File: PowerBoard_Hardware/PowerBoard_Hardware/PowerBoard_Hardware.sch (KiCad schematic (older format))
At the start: 12 parts

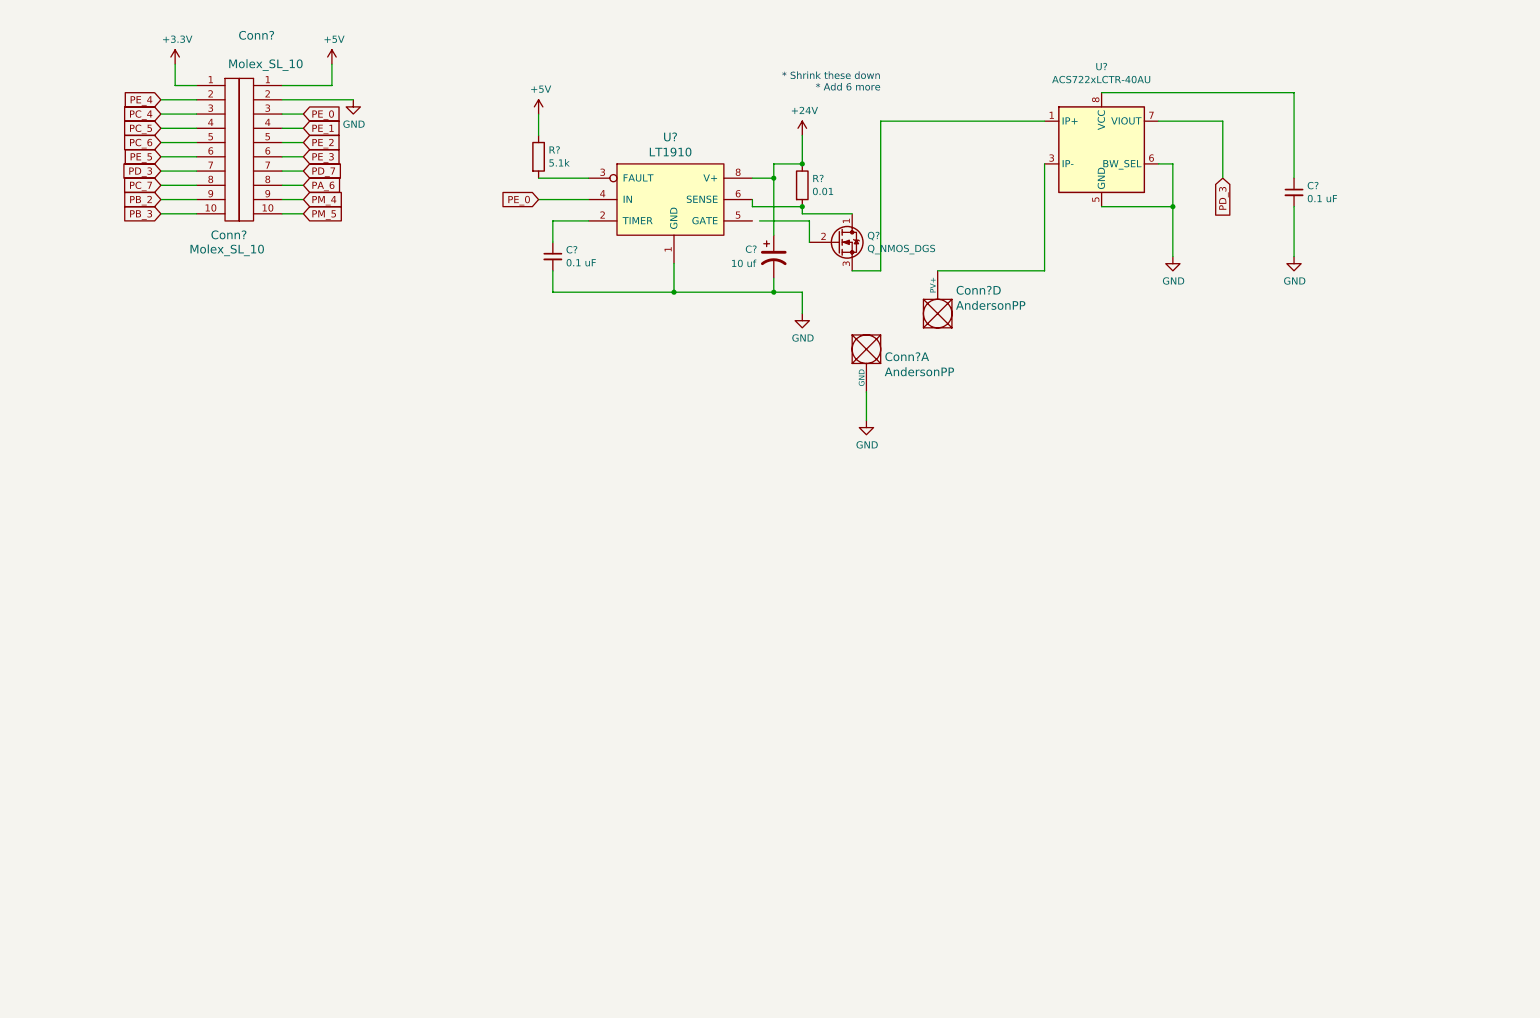
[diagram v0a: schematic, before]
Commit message: Pass 1.2
*Circuit has been consolidated
*All 6 circuits have been added
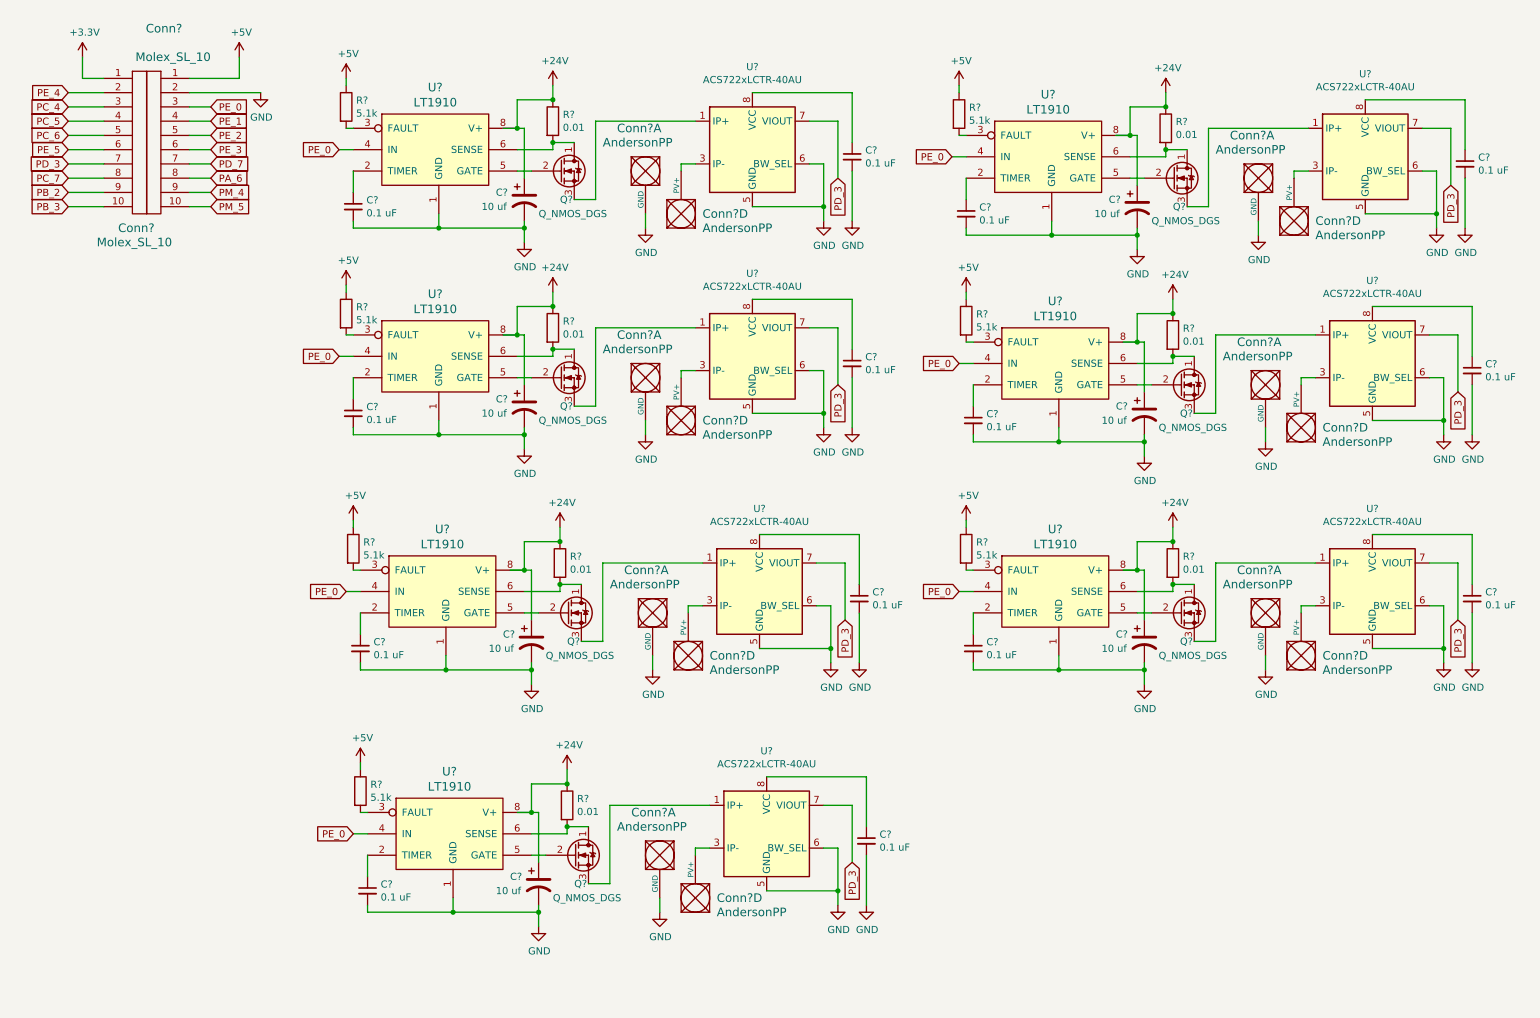
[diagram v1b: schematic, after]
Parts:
- added C? (x12): 0.1 uF, symbol Device:C_Small
- added C? (x6): 10 uf, symbol Device:CP1
- added Conn? (x12): AndersonPP, symbol MRDT_Connectors:AndersonPP
- added Q? (x6): Q_NMOS_DGS, symbol Device:Q_NMOS_DGS
- added R? (x6): 5.1k, symbol Device:R
- added R? (x6): 0.01, symbol Device:R
- added U? (x6): ACS722xLCTR-40AU, Package_SO:SOIC-8_3.9x4.9mm_P1.27mm, symbol Sensor_Current:ACS722xLCTR-40AU
- added U? (x6): LT1910, symbol MRDT_ICs:LT1910
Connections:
- net +24V: now also C?.1, C?.1, C?.1, C?.1, C?.1, C?.1, R?.1, R?.1, R?.1, R?.1, R?.1, R?.1, U?.8 (V+), U?.8 (V+), U?.8 (V+), U?.8 (V+), U?.8 (V+), U?.8 (V+)
- net +5V: now also R?.1, R?.1, R?.1, R?.1, R?.1, R?.1
- net GND: now also C?.2, C?.2, C?.2, C?.2, C?.2, C?.2, C?.2, C?.2, C?.2, C?.2, C?.2, C?.2, C?.2, C?.2, C?.2, C?.2, C?.2, C?.2, Conn?.1 (GND), Conn?.1 (GND), Conn?.1 (GND), Conn?.1 (GND), Conn?.1 (GND), Conn?.1 (GND), U?.1 (GND), U?.1 (GND), U?.1 (GND), U?.1 (GND), U?.1 (GND), U?.1 (GND), U?.5 (GND), U?.5 (GND), U?.5 (GND), U?.5 (GND), U?.5 (GND), U?.5 (GND), U?.6 (BW_SEL), U?.6 (BW_SEL), U?.6 (BW_SEL), U?.6 (BW_SEL), U?.6 (BW_SEL), U?.6 (BW_SEL)
- net PD_3: now also U?.7 (VIOUT), U?.7 (VIOUT), U?.7 (VIOUT), U?.7 (VIOUT), U?.7 (VIOUT), U?.7 (VIOUT)
- net PE_0: now also U?.4 (IN), U?.4 (IN), U?.4 (IN), U?.4 (IN), U?.4 (IN), U?.4 (IN)
- net at U?.5 (GATE): now also Q?.2 (G)
- new net: Q?.3 (S), U?.1 (IP+), U?.2 (IP+) (x6)
- new net: Conn?.4 (PV+), U?.3 (IP-), U?.4 (IP-) (x6)
- new net: C?.1, U?.8 (VCC) (x6)
- new net: R?.2, U?.3 (FAULT) (x6)
- new net: Q?.1 (D), R?.2, U?.6 (SENSE) (x6)
- new net: C?.1, U?.2 (TIMER) (x6)
- new net: Q?.2 (G), U?.5 (GATE) (x6)
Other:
- note removed: "* Shrink these down\n* Add 6 more\n"
- moved on the sheet: C?, Conn?, Conn?A, Conn?D, Q?, R?, U?

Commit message: Pass 1.3
*+24v replaced with VDD
*Analog pins assigned
*global PV Andersons assigned
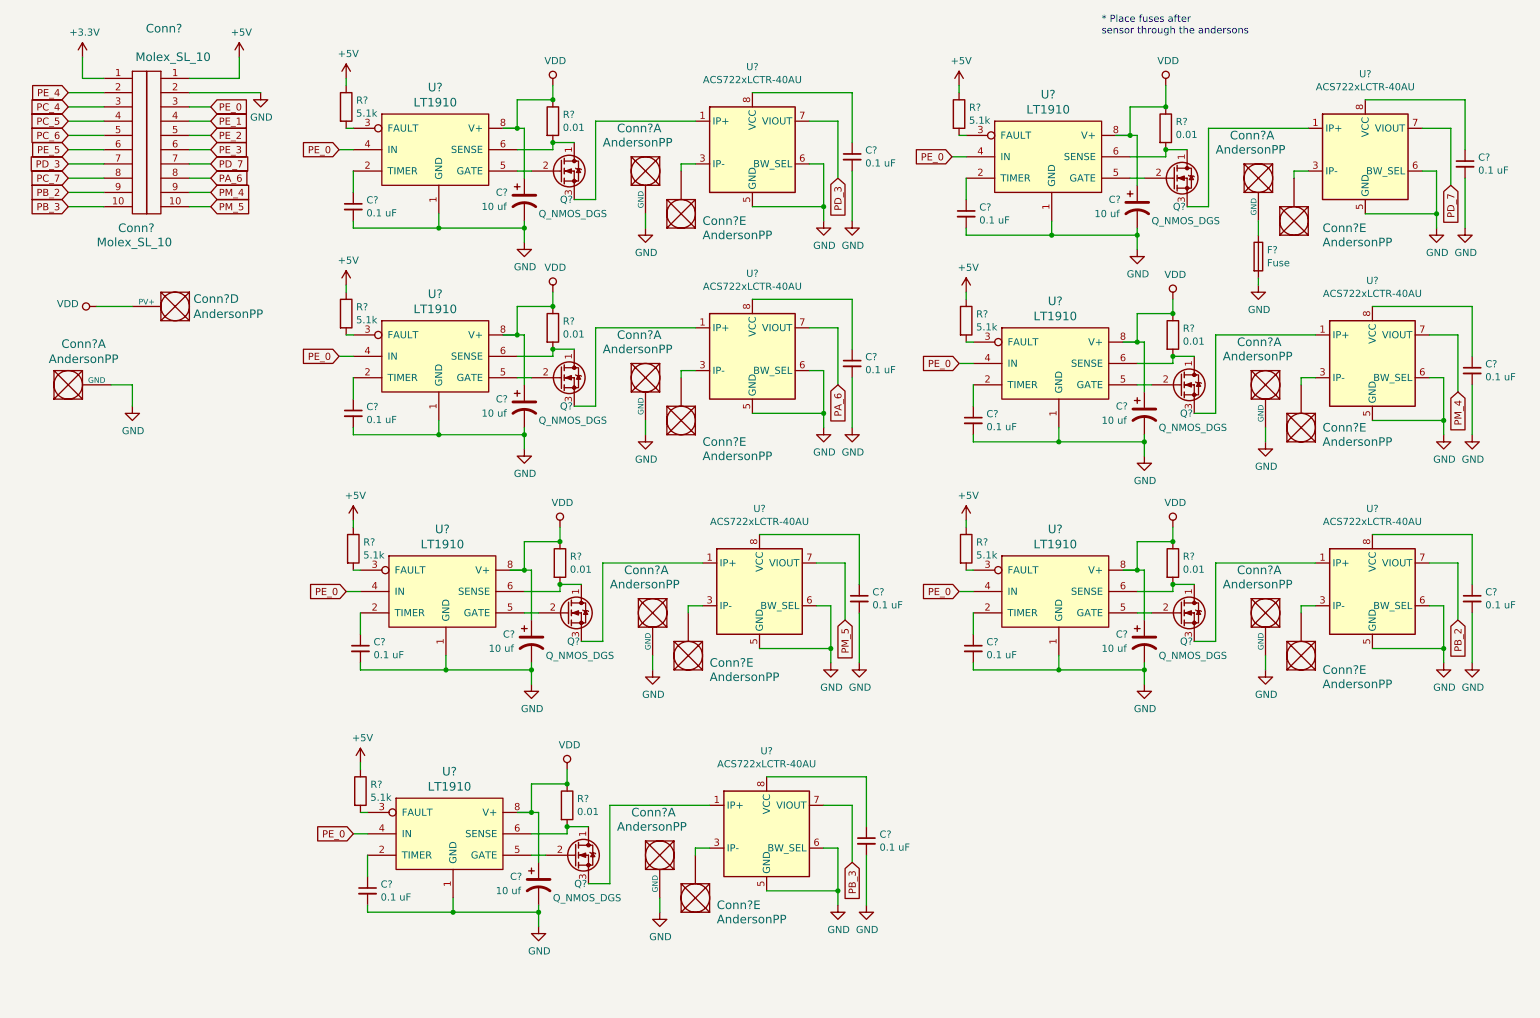
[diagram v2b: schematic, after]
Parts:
- removed Conn? (x7): AndersonPP, symbol MRDT_Connectors:AndersonPP
- added Conn? (x9): AndersonPP, symbol MRDT_Connectors:AndersonPP
- added F?: Fuse, symbol Device:Fuse
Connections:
- net GND: now also Conn?.1 (GND), F?.2; no longer Conn?.1 (GND)
- net PA_6: now also U?.7 (VIOUT)
- net PB_2: now also U?.7 (VIOUT)
- net PB_3: now also U?.7 (VIOUT)
- net PD_3: no longer U?.7 (VIOUT), U?.7 (VIOUT), U?.7 (VIOUT), U?.7 (VIOUT), U?.7 (VIOUT), U?.7 (VIOUT)
- net PD_7: now also U?.7 (VIOUT)
- net PM_4: now also U?.7 (VIOUT)
- net PM_5: now also U?.7 (VIOUT)
- net at U?.3 (IP-), U?.4 (IP-): now also Conn?.1 (x7)
- net +24V renamed VDD
- net VDD: now also Conn?.4 (PV+)
- new net: Conn?.1 (GND), F?.1
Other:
- note added: "* Place fuses after \nsensor through the andersons\n"

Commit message: Pass 1.4
*Fuses have been added after each anderson
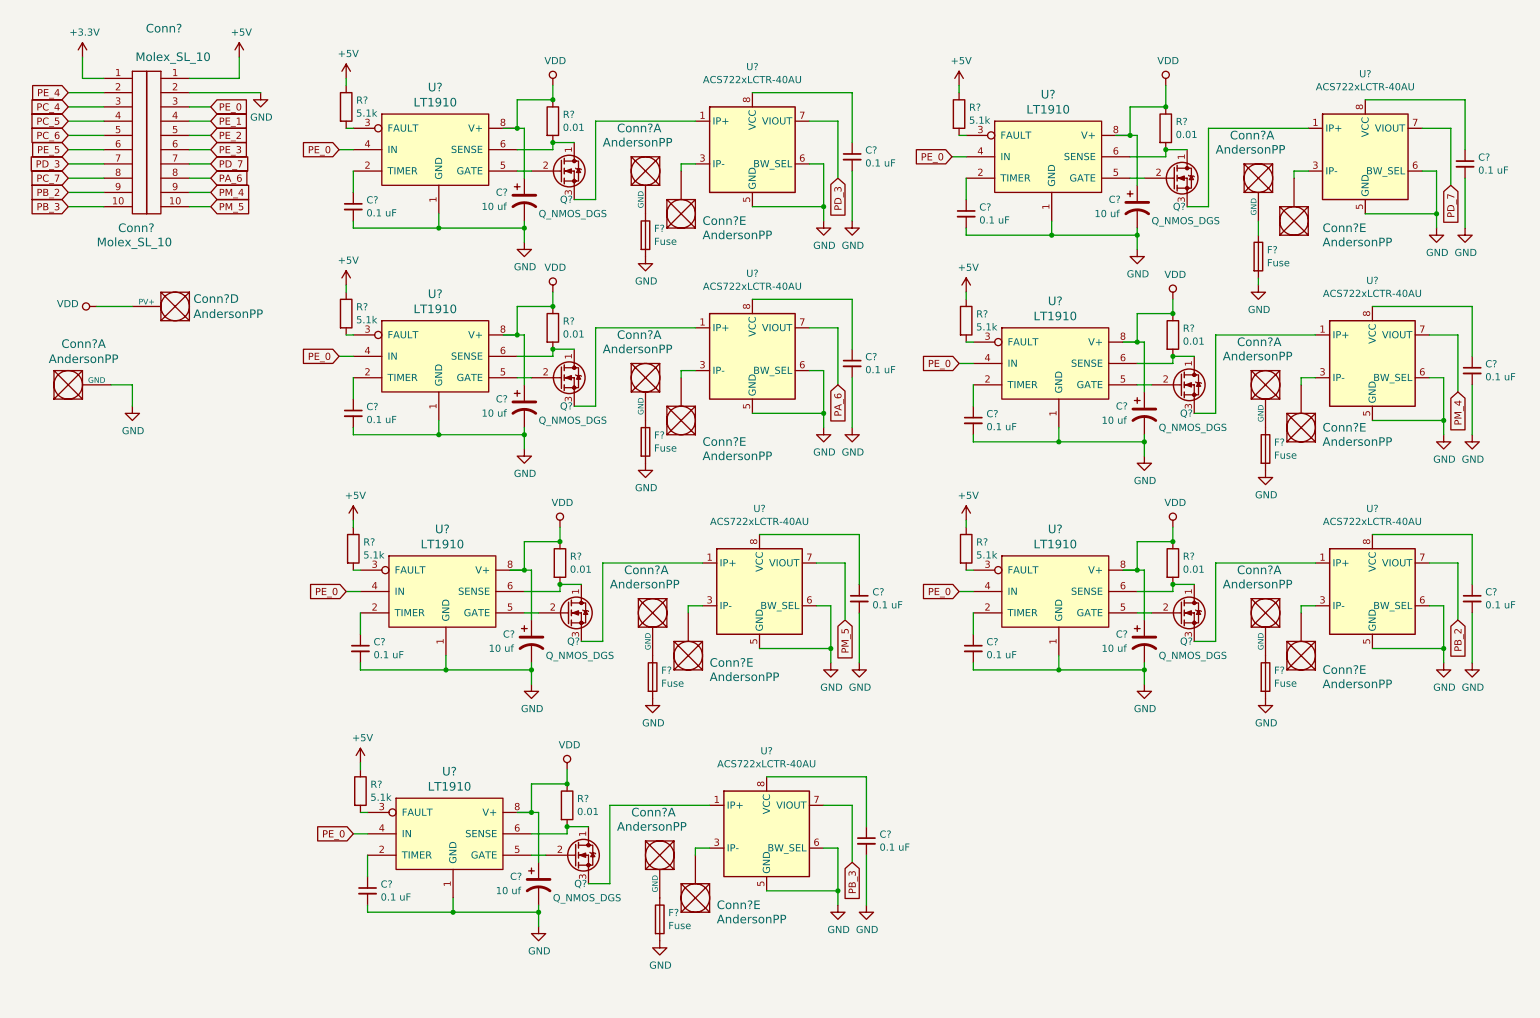
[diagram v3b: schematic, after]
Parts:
- added F? (x6): Fuse, symbol Device:Fuse
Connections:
- net GND: now also F?.2, F?.2, F?.2, F?.2, F?.2, F?.2; no longer Conn?.1 (GND), Conn?.1 (GND), Conn?.1 (GND), Conn?.1 (GND), Conn?.1 (GND), Conn?.1 (GND)
- new net: Conn?.1 (GND), F?.1 (x6)
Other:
- note removed: "* Place fuses after \nsensor through the andersons\n"
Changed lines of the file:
@@
 L power:GND #PWR?
 U 1 1 5D97EA33
-P 4950 2250
-F 0 "#PWR?" H 4950 2000 50  0001 C CNN
-F 1 "GND" H 4955 2077 50  0000 C CNN
-F 2 "" H 4950 2250 50  0001 C CNN
-F 3 "" H 4950 2250 50  0001 C CNN
-	1    4950 2250
+P 4950 2450
+F 0 "#PWR?" H 4950 2200 50  0001 C CNN
+F 1 "GND" H 4955 2277 50  0000 C CNN
+F 2 "" H 4950 2450 50  0001 C CNN
+F 3 "" H 4950 2450 50  0001 C CNN
+	1    4950 2450
 	1    0    0    -1
 $EndComp
@@
 Wire Wire Line
 	5200 1800 5200 1850
-Wire Wire Line
-	4950 2150 4950 2250
 Wire Wire Line
 	6200 2200 6200 2100
@@
 L power:GND #PWR?
 U 1 1 5D9E1C40
-P 4950 3700
-F 0 "#PWR?" H 4950 3450 50  0001 C CNN
-F 1 "GND" H 4955 3527 50  0000 C CNN
-F 2 "" H 4950 3700 50  0001 C CNN
-F 3 "" H 4950 3700 50  0001 C CNN
-	1    4950 3700
+P 4950 3900
+F 0 "#PWR?" H 4950 3650 50  0001 C CNN
+F 1 "GND" H 4955 3727 50  0000 C CNN
+F 2 "" H 4950 3900 50  0001 C CNN
+F 3 "" H 4950 3900 50  0001 C CNN
+	1    4950 3900
 	1    0    0    -1
 $EndComp
@@
 Wire Wire Line
 	5200 3250 5200 3300
-Wire Wire Line
-	4950 3600 4950 3700
 Wire Wire Line
 	6200 3650 6200 3550
@@
 L power:GND #PWR?
 U 1 1 5DA221E1
-P 9300 3750
-F 0 "#PWR?" H 9300 3500 50  0001 C CNN
-F 1 "GND" H 9305 3577 50  0000 C CNN
-F 2 "" H 9300 3750 50  0001 C CNN
-F 3 "" H 9300 3750 50  0001 C CNN
-	1    9300 3750
+P 9300 3950
+F 0 "#PWR?" H 9300 3700 50  0001 C CNN
+F 1 "GND" H 9305 3777 50  0000 C CNN
+F 2 "" H 9300 3950 50  0001 C CNN
+F 3 "" H 9300 3950 50  0001 C CNN
+	1    9300 3950
 	1    0    0    -1
 $EndComp
@@
 Wire Wire Line
 	9550 3300 9550 3350
-Wire Wire Line
-	9300 3650 9300 3750
 Wire Wire Line
 	10550 3700 10550 3600
@@
 L power:GND #PWR?
 U 1 1 5DA2DAD8
-P 5000 5350
-F 0 "#PWR?" H 5000 5100 50  0001 C CNN
-F 1 "GND" H 5005 5177 50  0000 C CNN
-F 2 "" H 5000 5350 50  0001 C CNN
-F 3 "" H 5000 5350 50  0001 C CNN
-	1    5000 5350
+P 5000 5550
+F 0 "#PWR?" H 5000 5300 50  0001 C CNN
+F 1 "GND" H 5005 5377 50  0000 C CNN
+F 2 "" H 5000 5550 50  0001 C CNN
+F 3 "" H 5000 5550 50  0001 C CNN
+	1    5000 5550
 	1    0    0    -1
 $EndComp
@@
 Wire Wire Line
 	5250 4900 5250 4950
-Wire Wire Line
-	5000 5250 5000 5350
 Wire Wire Line
 	6250 5300 6250 5200
@@
 L power:GND #PWR?
 U 1 1 5DA4370E
-P 9300 5350
-F 0 "#PWR?" H 9300 5100 50  0001 C CNN
-F 1 "GND" H 9305 5177 50  0000 C CNN
-F 2 "" H 9300 5350 50  0001 C CNN
-F 3 "" H 9300 5350 50  0001 C CNN
-	1    9300 5350
+P 9300 5550
+F 0 "#PWR?" H 9300 5300 50  0001 C CNN
+F 1 "GND" H 9305 5377 50  0000 C CNN
+F 2 "" H 9300 5550 50  0001 C CNN
+F 3 "" H 9300 5550 50  0001 C CNN
+	1    9300 5550
 	1    0    0    -1
 $EndComp
@@
 Wire Wire Line
 	9550 4900 9550 4950
-Wire Wire Line
-	9300 5250 9300 5350
 Wire Wire Line
 	10550 5300 10550 5200
@@
 L power:GND #PWR?
 U 1 1 5DA59E26
-P 5050 7050
-F 0 "#PWR?" H 5050 6800 50  0001 C CNN
-F 1 "GND" H 5055 6877 50  0000 C CNN
-F 2 "" H 5050 7050 50  0001 C CNN
-F 3 "" H 5050 7050 50  0001 C CNN
-	1    5050 7050
+P 5050 7250
+F 0 "#PWR?" H 5050 7000 50  0001 C CNN
+F 1 "GND" H 5055 7077 50  0000 C CNN
+F 2 "" H 5050 7250 50  0001 C CNN
+F 3 "" H 5050 7250 50  0001 C CNN
+	1    5050 7250
 	1    0    0    -1
 $EndComp
@@
 Wire Wire Line
 	5300 6600 5300 6650
-Wire Wire Line
-	5050 6950 5050 7050
 Wire Wire Line
 	6300 7000 6300 6900
@@
 Wire Wire Line
 	9250 2300 9250 2200
-Text Notes 8150 900  0    50   ~ 0
-* Place fuses after \nsensor through the andersons\n
 Wire Wire Line
 	1350 3350 1350 3500
@@
 	0    -1   -1   0
 $EndComp
+$Comp
+L Device:Fuse F?
+U 1 1 5DA6C5B0
+P 4950 2300
+F 0 "F?" H 5010 2346 50  0000 L CNN
+F 1 "Fuse" H 5010 2255 50  0000 L CNN
+F 2 "" V 4880 2300 50  0001 C CNN
+F 3 "~" H 4950 2300 50  0001 C CNN
+	1    4950 2300
+	1    0    0    -1
+$EndComp
+$Comp
+L Device:Fuse F?
+U 1 1 5DA6E34F
+P 4950 3750
+F 0 "F?" H 5010 3796 50  0000 L CNN
+F 1 "Fuse" H 5010 3705 50  0000 L CNN
+F 2 "" V 4880 3750 50  0001 C CNN
+F 3 "~" H 4950 3750 50  0001 C CNN
+	1    4950 3750
+	1    0    0    -1
+$EndComp
+$Comp
+L Device:Fuse F?
+U 1 1 5DA6EE41
+P 9300 3800
+F 0 "F?" H 9360 3846 50  0000 L CNN
+F 1 "Fuse" H 9360 3755 50  0000 L CNN
+F 2 "" V 9230 3800 50  0001 C CNN
+F 3 "~" H 9300 3800 50  0001 C CNN
+	1    9300 3800
+	1    0    0    -1
+$EndComp
+$Comp
+L Device:Fuse F?
+U 1 1 5DA707BE
+P 9300 5400
+F 0 "F?" H 9360 5446 50  0000 L CNN
+F 1 "Fuse" H 9360 5355 50  0000 L CNN
+F 2 "" V 9230 5400 50  0001 C CNN
+F 3 "~" H 9300 5400 50  0001 C CNN
+	1    9300 5400
+	1    0    0    -1
+$EndComp
+$Comp
+L Device:Fuse F?
+U 1 1 5DA72311
+P 5000 5400
+F 0 "F?" H 5060 5446 50  0000 L CNN
+F 1 "Fuse" H 5060 5355 50  0000 L CNN
+F 2 "" V 4930 5400 50  0001 C CNN
+F 3 "~" H 5000 5400 50  0001 C CNN
+	1    5000 5400
+	1    0    0    -1
+$EndComp
+$Comp
+L Device:Fuse F?
+U 1 1 5DA738C2
+P 5050 7100
+F 0 "F?" H 5110 7146 50  0000 L CNN
+F 1 "Fuse" H 5110 7055 50  0000 L CNN
+F 2 "" V 4980 7100 50  0001 C CNN
+F 3 "~" H 5050 7100 50  0001 C CNN
+	1    5050 7100
+	1    0    0    -1
+$EndComp
 $EndSCHEMATC
